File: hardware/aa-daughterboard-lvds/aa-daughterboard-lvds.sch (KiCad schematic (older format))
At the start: 107 parts, among them CN1 Barrel_Jack, CN10 6P6C, CN11 6P6C, CN12 6P6C, CN13 6P6C, CN14 Conn_01x08, CN15 Conn_01x08, CN16 Conn_01x08, CN17 8P8C, CN18 8P8C, CN19 8P8C, CN2 Conn_01x02, CN3 Conn_01x03, CN4 Conn_01x03, CN5 6P6C, CN6 Conn_01x04, CN7 Conn_01x04, CN8 Conn_01x04, CN9 Conn_01x04, P1 Conn_02x25_Odd_Even, P2 Conn_02x25_Odd_Even, Q1 TN1610H, U1 24LC08, U2 NIS5132xx, U3 uA7805, U4 75ALS192, U5 75ALS192, U6 75ALS192, U7 75ALS192, U8 75ALS192

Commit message: Rough grouping of components done
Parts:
- Q1: footprint Package_TO_SOT_THT:TO-220-3_Horizontal_TabDown -> Package_TO_SOT_THT:TO-220-3_Vertical
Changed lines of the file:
@@
 F 0 "Q1" H 2788 2546 50  0000 L CNN
 F 1 "TN1610H" H 2788 2455 50  0000 L CNN
-F 2 "Package_TO_SOT_THT:TO-220-3_Horizontal_TabDown" V 2700 2500 50  0001 C CNN
+F 2 "Package_TO_SOT_THT:TO-220-3_Vertical" V 2700 2500 50  0001 C CNN
 F 3 "~" V 2700 2500 50  0001 C CNN
 	1    2700 2500

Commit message: Add STM32 symbols... I don't think I have this right yet
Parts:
- removed P1, P2: Conn_02x25_Odd_Even, Connector_PinSocket_2.54mm:PinSocket_2x25_P2.54mm_Vertical, symbol Connector_Generic:Conn_02x25_Odd_Even
- added DISCO1: STM32F407_Discovery_P1, aa-daughterboard-lvds:STM32F407_Discovery_P1_P2_Socket, symbol aa-daughterboard-lvds:STM32F407_Discovery_P1
- added R16, R17, R18, R19, R20, R21, R22, R23, R24, R25, R26, R27, R28, R29, R30, R31, R32, R33, R34, R35, R36, R37, R38, R39, R40, R41, R42, R43, R44, R45, R46, R47, R48, R49, R50, R51, R52, R53, R54, R55: 56, Resistor_SMD:R_0603_1608Metric, symbol Device:R
- added TP21: TestPoint, TestPoint:TestPoint_THTPad_D1.0mm_Drill0.5mm, symbol Connector:TestPoint
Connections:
- net labels removed: B00T0, PA0, PA1, PA10, PA13, PA14, PA15, PA2, PA3, PA4, PA5, PA6, PA7, PA8, PA9, PB0, PB1, PB10, PB11, PB12, PB13, PB14, PB15, PB2, PB3, PB4, PB5, PB6, PB7, PB8, PB9, PC0, PC1, PC10, PC11, PC12, PC13, PC14, PC15, PC2, PC3, PC4, PC5, PC6, PC7, PC8, PC9, PD0, PD1, PD10, PD11, PD12, PD13, PD14, PD15, PD2, PD3, PD4, PD5, PD6, PD7, PD8, PD9, PE0, PE1, PE10, PE11, PE12, PE13, PE14, PE15, PE2, PE3, PE4, PE5, PE6, PE7, PE8, PE9, PH0, PH1
- wire segments 832 -> 841
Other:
- moved on the sheet: C12, C13, C14, C6, C7, JP1, JP4, JP6, TP1, TP19, TP2, TP20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

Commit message: Name differential pairs, convert inconvenient 1x8 connectors to 2x4
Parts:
- removed DISCO1: STM32F407_Discovery_P1, aa-daughterboard-lvds:STM32F407_Discovery_P1_P2_Socket, symbol aa-daughterboard-lvds:STM32F407_Discovery_P1
- removed TP3, TP4: TestPoint, TestPoint:TestPoint_THTPad_D1.0mm_Drill0.5mm, symbol Connector:TestPoint
- added A1: STM32F407_Discovery_P1_P2, aa-daughterboard-lvds:STM32F407_Discovery_P1_P2_Socket, symbol aa-daughterboard-lvds:STM32F407_Discovery_P1_P2
- CN14, CN15, CN16: footprint Connector_PinHeader_2.54mm:PinHeader_1x08_P2.54mm_Vertical -> Connector_PinHeader_2.54mm:PinHeader_2x04_P2.54mm_Vertical
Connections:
- net labels added: PWM_CAP_1_N, PWM_CAP_1_P, PWM_CAP_2_N, PWM_CAP_2_P, PWM_CAP_A_N, PWM_CAP_A_P, PWM_CAP_B_N, PWM_CAP_B_P, RX_DEBUG_S, RX_INPUT_S, TX_DEBUG_S, TX_INPUT_S, TX_PANEL_0_N, TX_PANEL_0_P, TX_PANEL_1_N, TX_PANEL_1_P, TX_PANEL_2_N, TX_PANEL_2_P, TX_PANEL_3_N, TX_PANEL_3_P, TX_PANEL_4_N, TX_PANEL_4_P, TX_PANEL_5_N, TX_PANEL_5_P, TX_PANEL_6_N, TX_PANEL_6_P, TX_PANEL_7_N, TX_PANEL_7_P, TX_STALK_1_N, TX_STALK_1_P, TX_STALK_2_N, TX_STALK_2_P, TX_STALK_A_N, TX_STALK_A_P, TX_STALK_B_N, TX_STALK_B_P, TX_XP_0_N, TX_XP_0_P, TX_XP_1_N, TX_XP_1_P, TX_XP_2_N, TX_XP_2_P, TX_XP_3_N, TX_XP_3_P
- wire segments 841 -> 839
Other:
- moved on the sheet: C12, C13, C14, C15, C16, C17, CN14, CN15, CN16, CN17, CN18, CN19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

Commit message: Routed, labeling done pending double check
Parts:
- removed JP2: SolderJumper_3_Bridged12, Jumper:SolderJumper-3_P1.3mm_Bridged2Bar12_RoundedPad1.0x1.5mm, symbol Jumper:SolderJumper_3_Bridged12
- removed JP3: SolderJumper_2_Open, Jumper:SolderJumper-2_P1.3mm_Open_RoundedPad1.0x1.5mm, symbol Jumper:SolderJumper_2_Open
- added H1, H2, H3, H4: MountingHole_Pad, MountingHole:MountingHole_4.3mm_M4_Pad_Via, symbol Mechanical:MountingHole_Pad
- added R56: 10k, Resistor_SMD:R_0603_1608Metric, symbol Device:R
- added TP22, TP23, TP24, TP25, TP26, TP27, TP28, TP29, TP3, TP30, TP31, TP4: TestPoint, TestPoint:TestPoint_THTPad_D1.0mm_Drill0.5mm, symbol Connector:TestPoint
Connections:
- net GND: now also H1.1, H2.1, H3.1, H4.1, TP22.1, TP23.1, TP24.1, TP25.1, TP26.1, TP27.1, TP28.1, TP29.1, TP3.1, TP31.1, TP4.1
- net at CN1.1, CN2.1 (Pin_1), F1.2: now also R56.1, TP30.1
- net at CN1.3: now also R56.2
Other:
- moved on the sheet: C1, C4, C5, CN1, CN2, D2, D3, F1, JP5, JP7, Q1, R1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

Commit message: Implement todos
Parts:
- removed CN3, CN4: Conn_01x03, Connector_PinHeader_2.54mm:PinHeader_1x03_P2.54mm_Vertical, symbol Connector_Generic:Conn_01x03
- removed JP1: SolderJumper_2_Open, Jumper:SolderJumper-2_P1.3mm_Bridged_RoundedPad1.0x1.5mm, symbol Jumper:SolderJumper_2_Bridged
- removed JP6: SolderJumper_2_Open, Jumper:SolderJumper-2_P1.3mm_Open_RoundedPad1.0x1.5mm, symbol Jumper:SolderJumper_2_Open
- added CN20, CN21, CN22, CN23, CN24: Conn_01x02, Connector_PinHeader_2.54mm:PinHeader_1x02_P2.54mm_Vertical, symbol Connector_Generic:Conn_01x02
- added CN3, CN4: Conn_01x06, Connector_PinHeader_2.54mm:PinHeader_1x06_P2.54mm_Vertical, symbol Connector_Generic:Conn_01x06
- added D20, D21: LED, LED_SMD:LED_0603_1608Metric, symbol Device:LED
- added D22: BZX79C5V1, Diode_THT:D_DO-35_SOD27_P7.62mm_Horizontal, symbol Device:D_Zener
- added R57: 2.2k, Resistor_SMD:R_0603_1608Metric, symbol Device:R
- added R58: 680, Resistor_SMD:R_0603_1608Metric, symbol Device:R
- added R59: 220, Resistor_SMD:R_0603_1608Metric, symbol Device:R
- TP1, TP10, TP11, TP12, TP13, TP14, TP15, TP16, TP17, TP18, TP19, TP2, TP20, TP21, TP22, TP23, TP24, TP25, TP26, TP27, TP28, TP29, TP3, TP30, TP31, TP4, TP5, TP6, TP7, TP8, TP9: footprint TestPoint:TestPoint_THTPad_D1.0mm_Drill0.5mm -> TestPoint:TestPoint_THTPad_D2.0mm_Drill1.0mm
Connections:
- net +5V: now also A1.P2_3 (5V_53), A1.P2_4 (5V_54), D21.2 (A), R59.1
- net GND: now also CN20.2 (Pin_2), CN21.2 (Pin_2), CN22.2 (Pin_2), CN23.2 (Pin_2), CN24.2 (Pin_2), CN3.1 (Pin_1), CN4.1 (Pin_1), R57.1, R58.1
- net RX_DEBUG_S: now also CN4.4 (Pin_4)
- net RX_INPUT_S: now also CN3.4 (Pin_4)
- net TX_DEBUG_S: now also CN4.5 (Pin_5)
- net TX_INPUT_S: now also CN3.5 (Pin_5)
- net VDD: now also CN20.1 (Pin_1), CN21.1 (Pin_1), CN22.1 (Pin_1), CN23.1 (Pin_1), CN24.1 (Pin_1), D20.2 (A); no longer A1.P2_22 (VDD_72)
- net at D2.2 (A), Q1.3 (G): now also D22.2 (A)
- net at A1.P1_3 (VDD_3): no longer A1.P1_4 (VDD_4)
- new net: D21.1 (K), R58.2
- new net: D22.1 (K), R59.2
- new net: D20.1 (K), R57.2
- no-connect marks 50 -> 59
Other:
- moved on the sheet: C1, C4, C5, CN1, CN2, D2, D3, F1, JP5, JP7, Q1, R1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

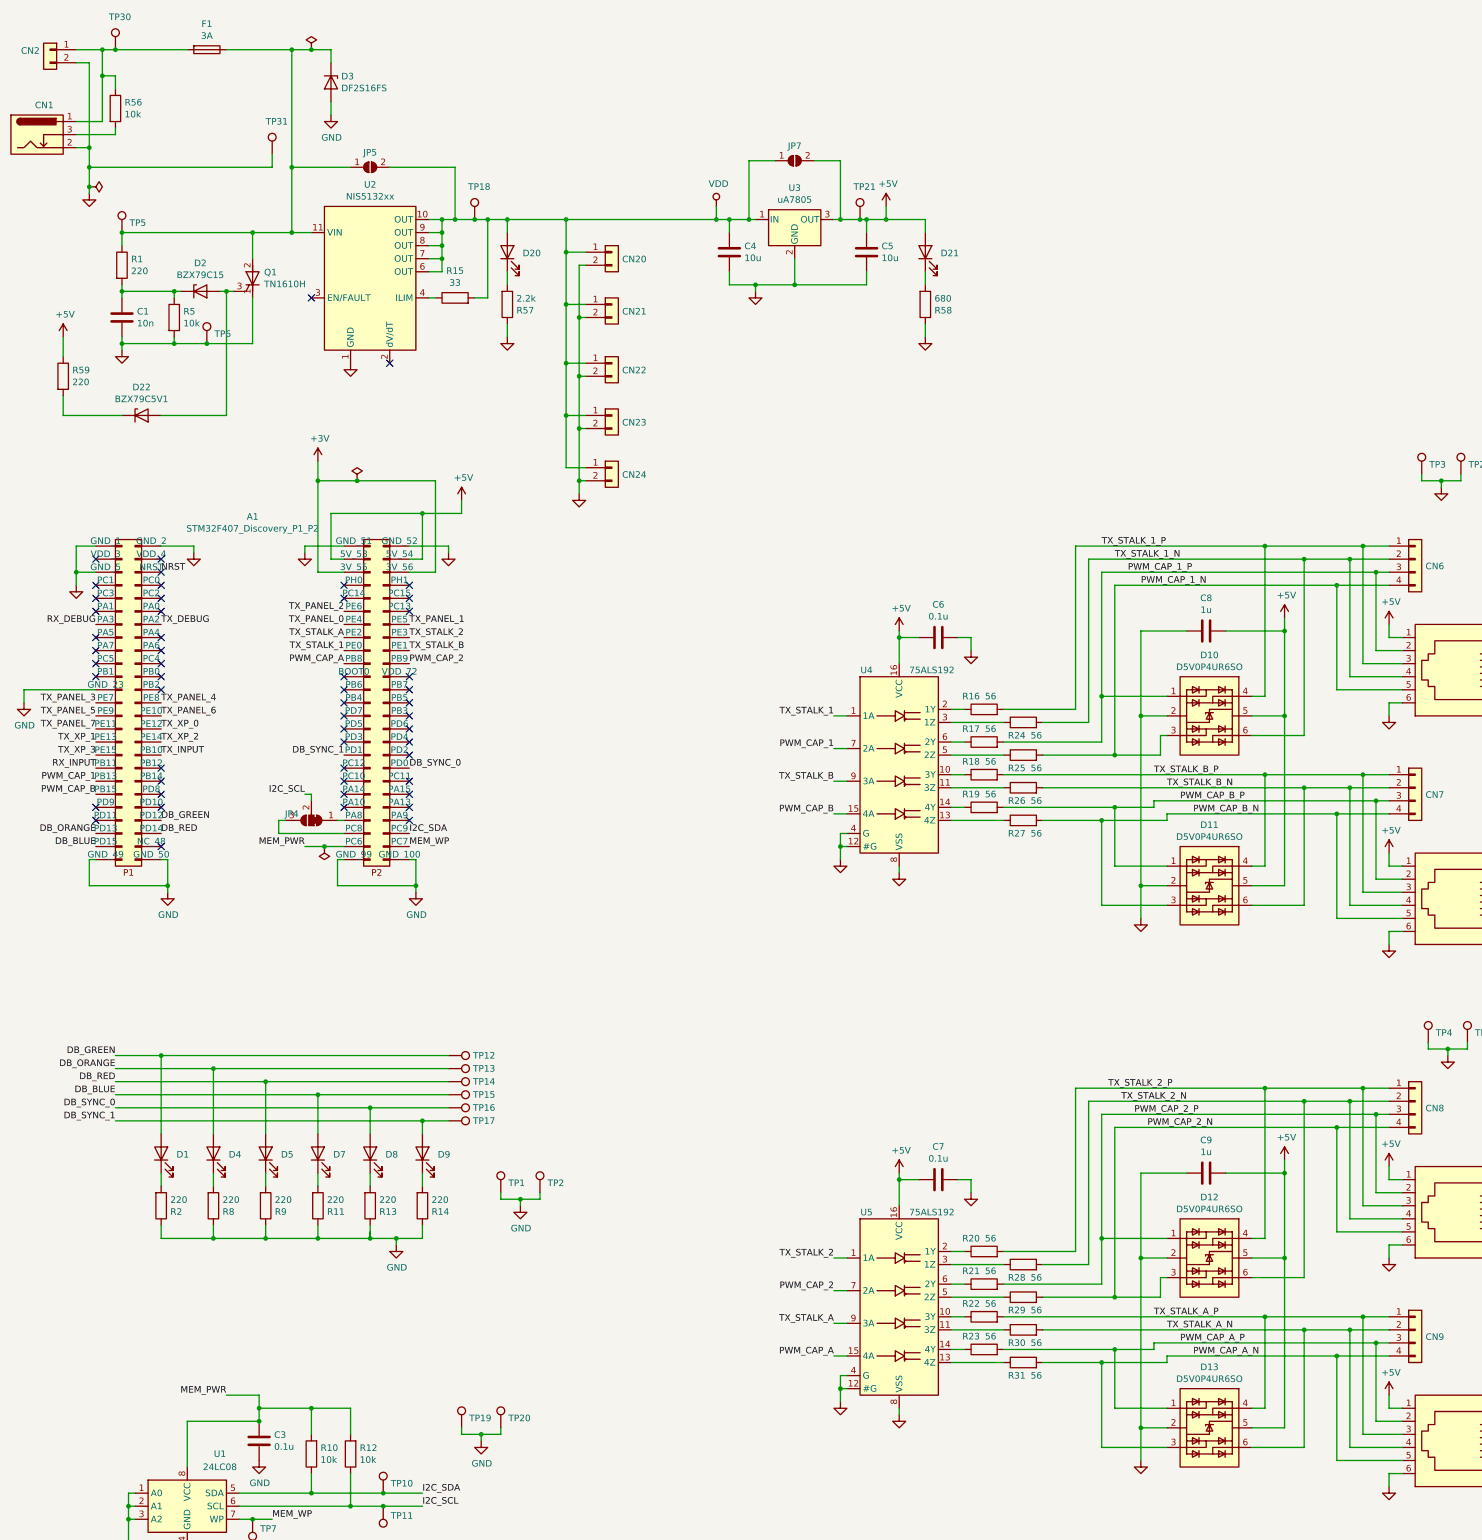
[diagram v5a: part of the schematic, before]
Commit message: More updates to daughterboard, begin panel receiver layout
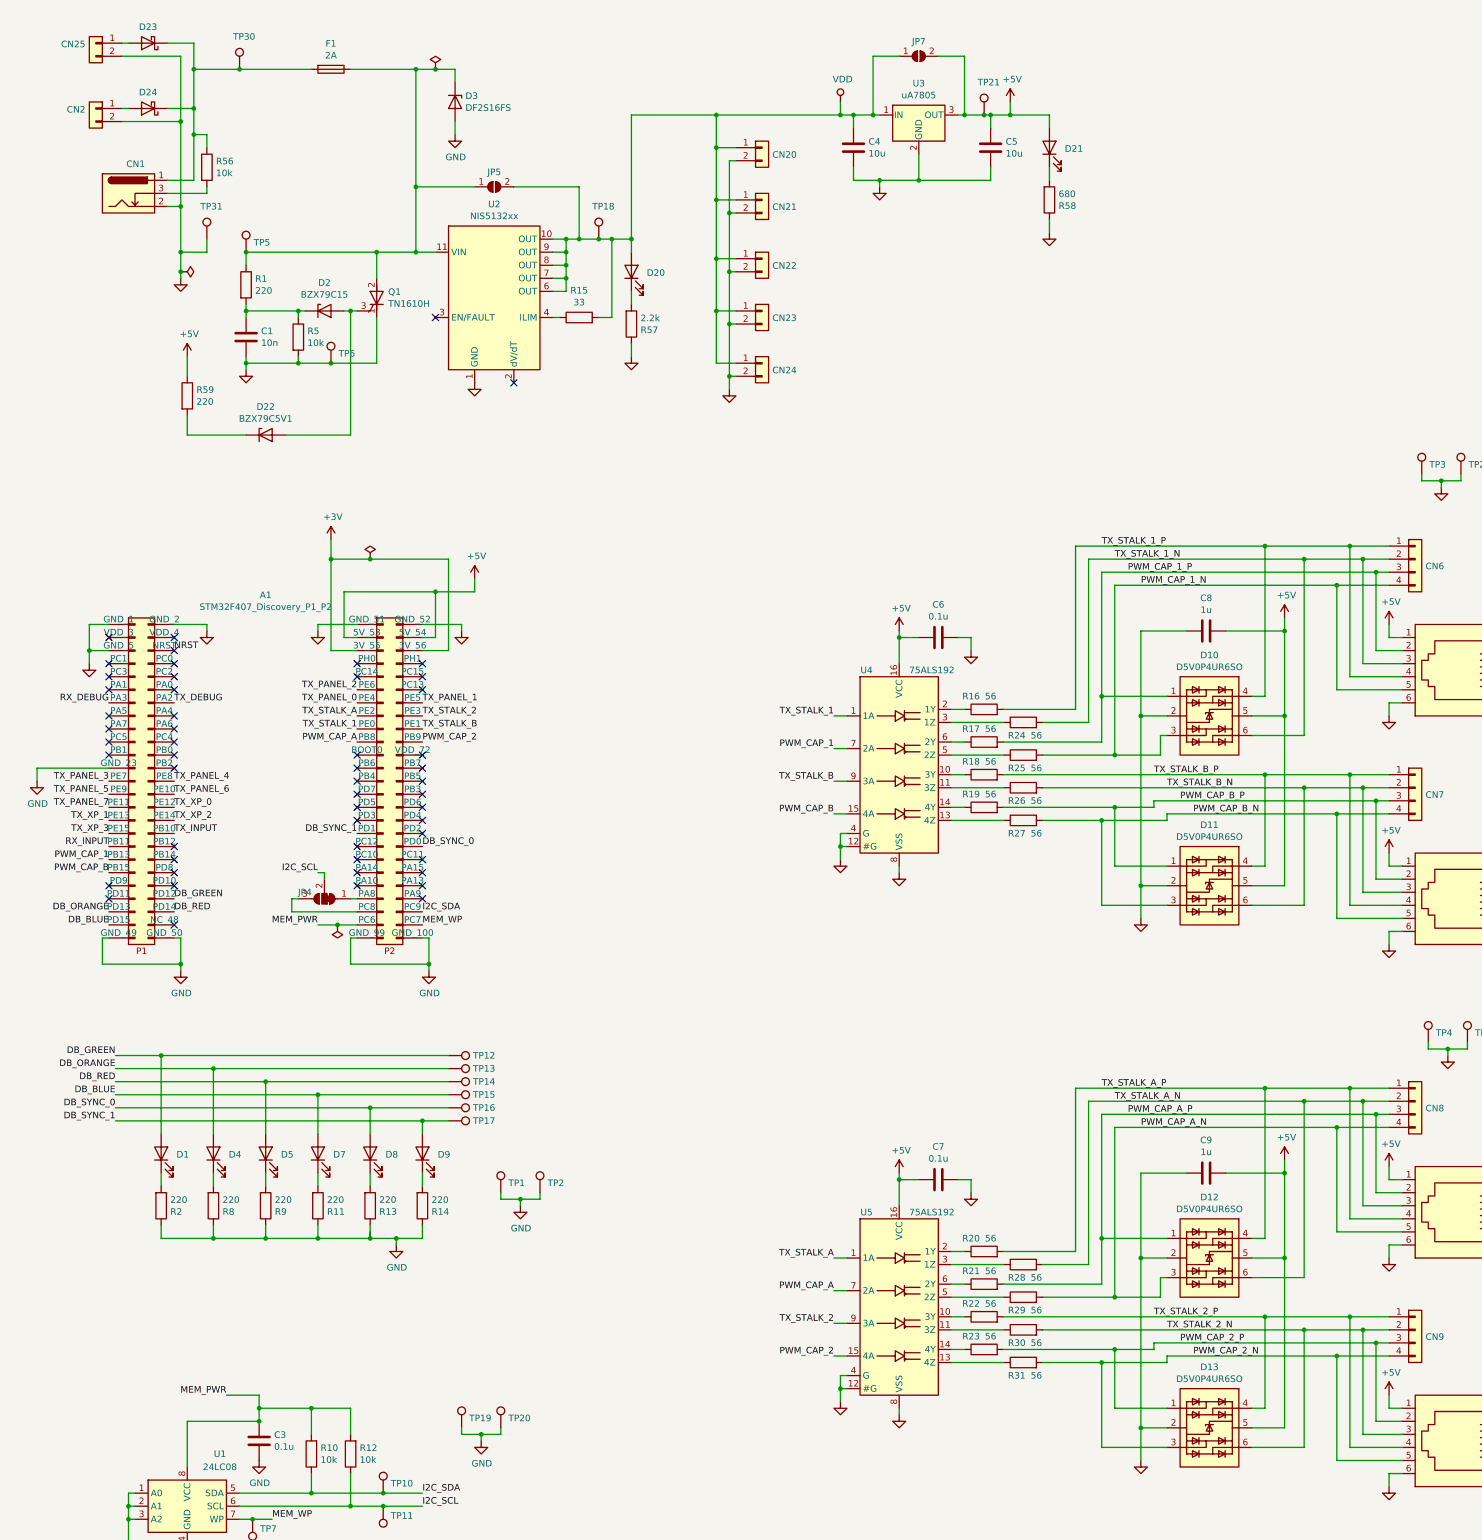
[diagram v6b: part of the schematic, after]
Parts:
- added CN25: Conn_01x02, Connector_Wire:SolderWirePad_1x02_P5.08mm_Drill1.5mm, symbol Connector_Generic:Conn_01x02
- added D23, D24: D_Schottky, aa-daughterboard-lvds:D_SOD-128, symbol Device:D_Schottky
- CN2: footprint Connector_Wire:SolderWirePad_1x02_P7.62mm_Drill2.5mm -> Connector_Wire:SolderWirePad_1x02_P5.08mm_Drill1.5mm
- F1: value 3A -> 2A
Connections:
- net GND: now also CN25.2 (Pin_2)
- net PWM_CAP_2: now also U5.15 (4A); no longer U5.7 (2A)
- net PWM_CAP_2_N: now also CN13.5, CN9.4 (Pin_4), D13.3 (K), R31.2; no longer CN12.5, CN8.4 (Pin_4), D12.3 (K), R29.2
- net PWM_CAP_2_P: now also CN13.2, CN9.3 (Pin_3), D13.1 (K), R23.2; no longer CN12.2, CN8.3 (Pin_3), D12.1 (K), R21.2
- net PWM_CAP_A: now also U5.7 (2A); no longer U5.15 (4A)
- net PWM_CAP_A_N: now also CN12.5, CN8.4 (Pin_4), D12.3 (K), R29.2; no longer CN13.5, CN9.4 (Pin_4), D13.3 (K), R31.2
- net PWM_CAP_A_P: now also CN12.2, CN8.3 (Pin_3), D12.1 (K), R21.2; no longer CN13.2, CN9.3 (Pin_3), D13.1 (K), R23.2
- net TX_STALK_1_N: now also CN10.3; no longer CN10.4
- net TX_STALK_1_P: now also CN10.4; no longer CN10.3
- net TX_STALK_2: now also U5.9 (3A); no longer U5.1 (1A)
- net TX_STALK_2_N: now also CN13.3, CN9.2 (Pin_2), D13.6 (K), R30.2; no longer CN12.4, CN8.2 (Pin_2), D12.6 (K), R28.2
- net TX_STALK_2_P: now also CN13.4, CN9.1 (Pin_1), D13.4 (K), R22.2; no longer CN12.3, CN8.1 (Pin_1), D12.4 (K), R20.2
- net TX_STALK_A: now also U5.1 (1A); no longer U5.9 (3A)
- net TX_STALK_A_N: now also CN12.3, CN8.2 (Pin_2), D12.6 (K), R28.2; no longer CN13.4, CN9.2 (Pin_2), D13.6 (K), R30.2
- net TX_STALK_A_P: now also CN12.4, CN8.1 (Pin_1), D12.4 (K), R20.2; no longer CN13.3, CN9.1 (Pin_1), D13.4 (K), R22.2
- net TX_STALK_B_N: now also CN11.3; no longer CN11.4
- net TX_STALK_B_P: now also CN11.4; no longer CN11.3
- net at CN1.1, F1.2, R56.1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: now also D23.1 (K), D24.1 (K); no longer CN2.1 (Pin_1)
- new net: CN2.1 (Pin_1), D24.2 (A)
- new net: CN25.1 (Pin_1), D23.2 (A)
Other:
- moved on the sheet: A1, C1, C4, C5, CN1, CN2, CN20, CN21, CN22, CN23, CN24, D2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
